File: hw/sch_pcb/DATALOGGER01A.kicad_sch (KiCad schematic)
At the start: 91 parts, among them J1 HEADER_2x01_PARALLEL, J10 HEADER_2x03_PARALLEL, J11 HEADER_2x01, J12 HEADER_2x01_PARALLEL, J13 HEADER_2x01_PARALLEL, J14 HEADER_2x01_PARALLEL, J15 HEADER_2x01_PARALLEL, J16 HEADER_2x01_PARALLEL, J17 HEADER_2x01_PARALLEL, J18 HEADER_2x01_PARALLEL, J19 HEADER_2x01_PARALLEL, J2 HEADER_2x01_PARALLEL, J20 HEADER_2x01_PARALLEL, J21 HEADER_2x01, J22 HEADER_2x01_PARALLEL, J23 HEADER_2x01_PARALLEL, J24 HEADER_2x01_PARALLEL, J25 HEADER_2x01_PARALLEL, J26 HEADER_2x01_PARALLEL, J27 HEADER_2x01_PARALLEL, J28 HEADER_2x01_PARALLEL, J29 HEADER_2x01_PARALLEL, J3 HEADER_2x01_PARALLEL, J30 HEADER_2x01_PARALLEL, J31 HEADER_2x03, J32 HEADER_2x01, J33 HEADER_2x03_PARALLEL, J34 MCC-SD (kouka z modulu), J4 HEADER_2x01_PARALLEL, J5 HEADER_2x01_PARALLEL, J6 HEADER_2x03_PARALLEL, J7 MCC-SD, J8 HEADER_2x01_PARALLEL, J9 HEADER_2x01, M1 HOLE, M2 HOLE, M3 HOLE, M4 HOLE, SW1 5MS1S102AM6QE, U1 ISL21080CIH320Z-TK, U2 TPS22965-Q1, U3 ATMEGA1284P-AU, U4 PCF85263A, U5 LM4041CIM3-1.2(neosazovat), U6 AT24CS64-SSHM, Y1 16MHz, Y2 ABS07-120-32.768KHZ-T

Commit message: Doplneni soucastek na osazovani
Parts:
- BT1, BT2: USD_ID (none) -> 5c70984412875079b91f87ed
- BT3: USD_ID (none) -> 5c70984412875079b91f87ec
- C1, C13, C15, C17, C18, C19, C2, C20, C21, C22, C3, C4, C5, C6, C8: USD_ID (none) -> 5c70984712875079b91f8b4c
- C11, C14: USD_ID (none) -> 5c70984812875079b91f8bbd
- C12: USD_ID (none) -> 5c70984712875079b91f8b45
- C16: USD_ID (none) -> 5c70984712875079b91f8b52
- C7: USD_ID (none) -> 5c70984712875079b91f8b50
- C9: USD_ID (none) -> 5c70984412875079b91f8867
- D2: USD_ID (none) -> 5c70984512875079b91f88ac
- D3: USD_ID (none) -> 5c70984712875079b91f8b67
- F1, F2: USD_ID (none) -> 5c70984512875079b91f88d2
- J7: USD_ID (none) -> 5c70984412875079b91f87f2
- L1: USD_ID (none) -> 5c70984412875079b91f87ff
- R1, R2, R3, R4: USD_ID (none) -> 5c70984512875079b91f8977
- R10: USD_ID (none) -> 5c70984612875079b91f8990
- R12, R15: USD_ID (none) -> 5c70984512875079b91f896b
- R5: USD_ID (none) -> 5c70984612875079b91f8995
- R6, R7, R9: USD_ID (none) -> 5c70984612875079b91f899f
- SW1: USD_ID (none) -> 5c70984712875079b91f8b66
- U1: USD_ID (none) -> 5c70984712875079b91f8b79
- U2: USD_ID (none) -> 5c70984712875079b91f8b78
- U3: USD_ID (none) -> 5c70984412875079b91f888e
- U4: USD_ID (none) -> 5c70984612875079b91f8a0c
- U6: USD_ID (none) -> 5c70984712875079b91f8b99
- Y1: USD_ID (none) -> 5c70984712875079b91f8b10
- Y2: USD_ID (none) -> 5c70984712875079b91f8b1b

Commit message: Doplnění součástek pro osazení
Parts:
- BT1, BT2: USD_ID 5c70984412875079b91f87ed -> (none); UST_ID (none) -> 5c70984412875079b91f87ed
- BT3: USD_ID 5c70984412875079b91f87ec -> (none); UST_ID (none) -> 5c70984412875079b91f87ec
- C1, C13, C15, C17, C18, C19, C2, C20, C21, C22, C3, C4, C5, C6, C8: USD_ID 5c70984712875079b91f8b4c -> (none); UST_ID (none) -> 5c70984712875079b91f8b4c
- C11, C14: USD_ID 5c70984812875079b91f8bbd -> (none); UST_ID (none) -> 5c70984812875079b91f8bbd
- C12: USD_ID 5c70984712875079b91f8b45 -> (none); UST_ID (none) -> 5c70984712875079b91f8b45
- C16: USD_ID 5c70984712875079b91f8b52 -> (none); UST_ID (none) -> 5c70984712875079b91f8b52
- C7: USD_ID 5c70984712875079b91f8b50 -> (none); UST_ID (none) -> 5c70984712875079b91f8b50
- C9: USD_ID 5c70984412875079b91f8867 -> (none); UST_ID (none) -> 5c70984412875079b91f8867
- D2: USD_ID 5c70984512875079b91f88ac -> (none); UST_ID (none) -> 5c70984512875079b91f88ac
- D3: USD_ID 5c70984712875079b91f8b67 -> (none); UST_ID (none) -> 5c70984712875079b91f8b67
- F1, F2: USD_ID 5c70984512875079b91f88d2 -> (none); UST_ID (none) -> 5c70984512875079b91f88d2
- J7: USD_ID 5c70984412875079b91f87f2 -> (none); UST_ID (none) -> 5c70984412875079b91f87f2
- L1: USD_ID 5c70984412875079b91f87ff -> (none); UST_ID (none) -> 5c70984412875079b91f87ff
- R1, R2, R3, R4: USD_ID 5c70984512875079b91f8977 -> (none); UST_ID (none) -> 5c70984512875079b91f8977
- R10: USD_ID 5c70984612875079b91f8990 -> (none); UST_ID (none) -> 5c70984612875079b91f8990
- R12, R15: USD_ID 5c70984512875079b91f896b -> (none); UST_ID (none) -> 5c70984512875079b91f896b
- R5: USD_ID 5c70984612875079b91f8995 -> (none); UST_ID (none) -> 5c70984612875079b91f8995
- R6, R7, R9: USD_ID 5c70984612875079b91f899f -> (none); UST_ID (none) -> 5c70984612875079b91f899f
- SW1: USD_ID 5c70984712875079b91f8b66 -> (none); UST_ID (none) -> 5c70984712875079b91f8b66
- U1: USD_ID 5c70984712875079b91f8b79 -> (none); UST_ID (none) -> 5c70984712875079b91f8b79
- U2: USD_ID 5c70984712875079b91f8b78 -> (none); UST_ID (none) -> 5c70984712875079b91f8b78
- U3: USD_ID 5c70984412875079b91f888e -> (none); UST_ID (none) -> 5c70984412875079b91f888e
- U4: USD_ID 5c70984612875079b91f8a0c -> (none); UST_ID (none) -> 5c70984612875079b91f8a0c
- U6: USD_ID 5c70984712875079b91f8b99 -> (none); UST_ID (none) -> 5c70984712875079b91f8b99
- Y1: USD_ID 5c70984712875079b91f8b10 -> (none); UST_ID (none) -> 5c70984712875079b91f8b10
- Y2: USD_ID 5c70984712875079b91f8b1b -> (none); UST_ID (none) -> 5c70984712875079b91f8b1b

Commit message: Edit SCH
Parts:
- C5, C8: value 100nF -> 15pF; UST_ID 5c70984712875079b91f8b4c -> 5c70984712875079b91f8b32

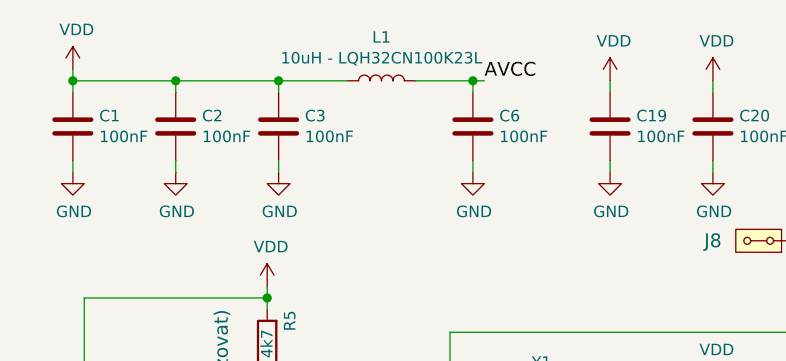
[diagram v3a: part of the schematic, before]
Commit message: Update schematics and title block.
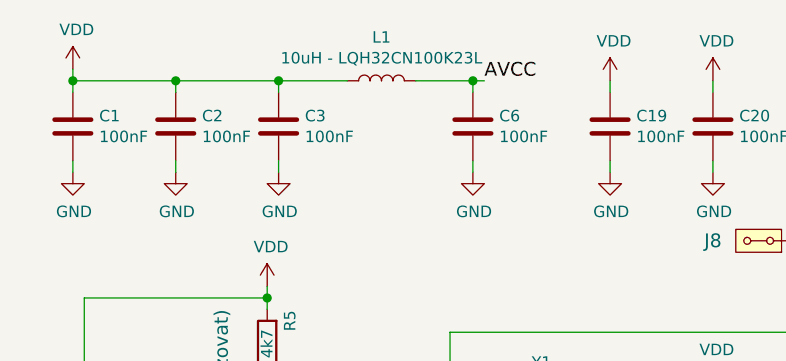
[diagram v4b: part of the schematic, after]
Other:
- title: NAME -> DATALOGGER01A
